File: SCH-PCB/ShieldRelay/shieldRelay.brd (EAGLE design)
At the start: 99.1 x 84.1 mm, 67 parts, among them IC1 LM2596SX-5.0_NOPB, IC2 LM1117MPX-33NOPB, K1 SLA-05VDC-SL-C, K2 SRD-05VDC-SL-C, K3 G3MB-202PL-DC5, K5 G3MB-202PL-DC5, K6 SRD-05VDC-SL-C, Q1 MMST2222A-7-F, Q2 MMST2222A-7-F, Q3 MMST2222A-7-F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

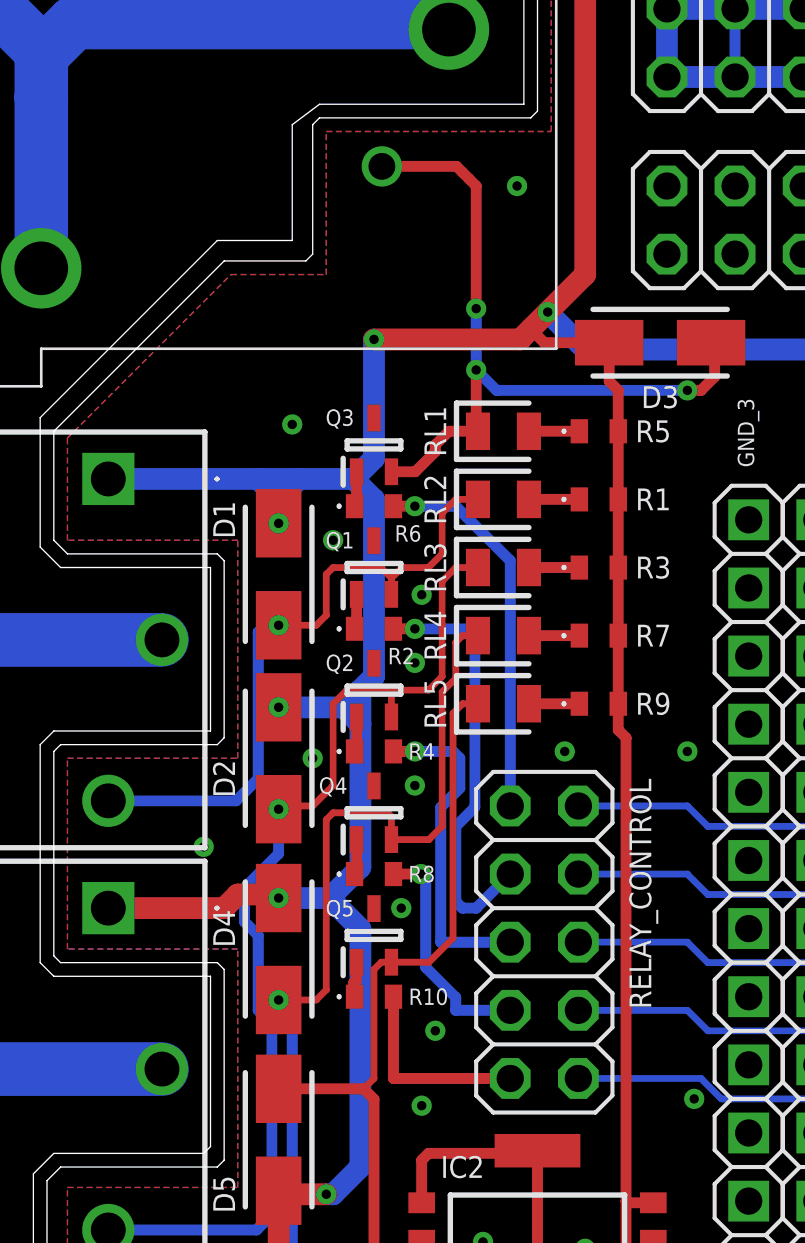
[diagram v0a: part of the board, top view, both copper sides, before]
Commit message: FIX: fix reverse transistor relay
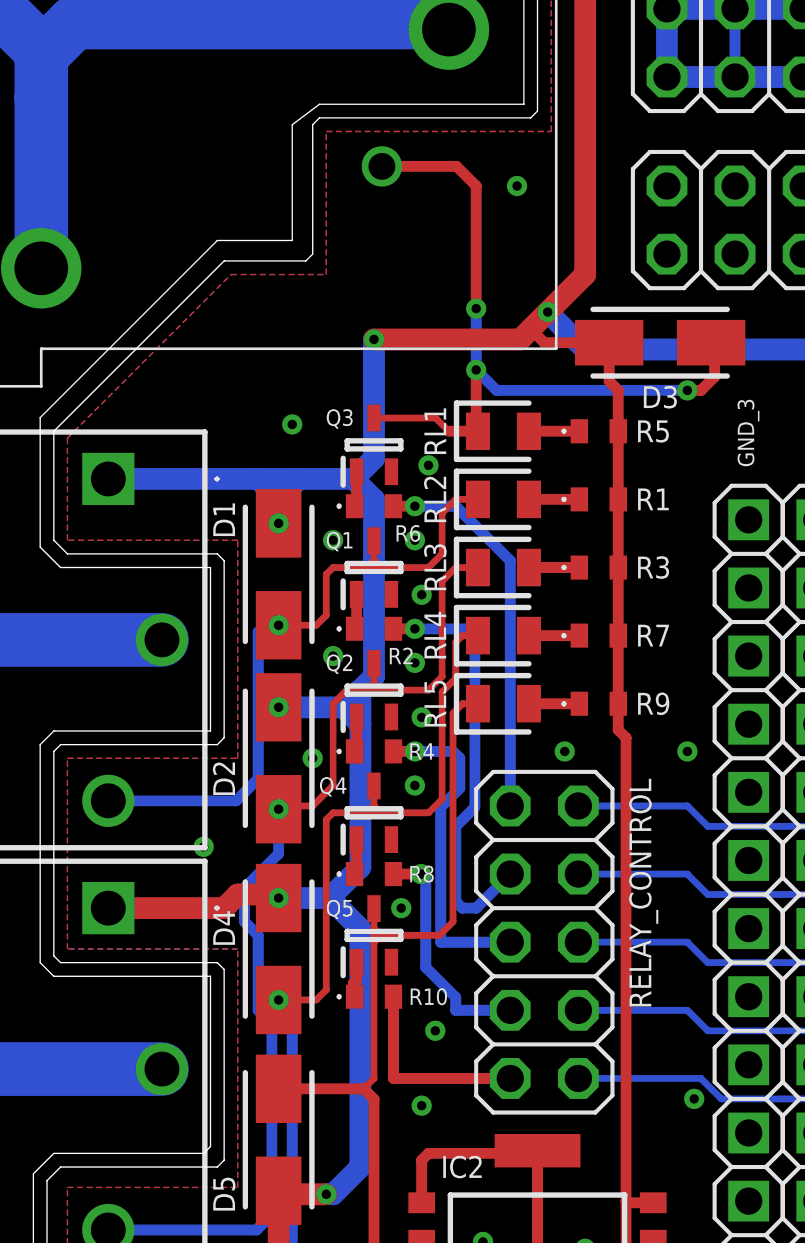
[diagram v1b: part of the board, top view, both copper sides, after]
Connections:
- net GND: now also Q1.2, Q2.2, Q3.2, Q4.2, Q5.2; no longer Q1.3, Q2.3, Q3.3, Q4.3, Q5.3
- net N$11: now also Q4.3; no longer Q4.2
- net N$14: now also Q5.3; no longer Q5.2
- net N$3: now also Q1.3; no longer Q1.2
- net N$5: now also Q2.3; no longer Q2.2
- net N$8: now also Q3.3; no longer Q3.2
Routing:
- net N$14: track 38.2 -> 40.3 mm
- net N$3: track 24.4 -> 24.9 mm
- net GND: vias 31 -> 35
